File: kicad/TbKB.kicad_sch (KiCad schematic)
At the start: 320 parts, among them U1 NCP1117-3.3_SOT223, U2 W25Q128JVS, U3 RP2040, X1 USB Type C, Y1 ABLS-12.000MHZ-B4-T

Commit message: routing complete
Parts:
- added K_Space_2U_2: SW_SPST, keyswitches:Kailh_socket_MX_2.25u, symbol Switch:SW_SPST
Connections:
- net Col_3: now also K_Space_2U_2.2 (B)
- net at D33.2 (A), K_enter1.1 (A): now also K_Space_2U_2.1 (A)
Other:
- note added: "Make sure R7 and R8 are close to RP2040"
- note removed: "Make sure R3 and R4 are close to RP2040"
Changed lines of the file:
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@@
   (junction (at 402.59 294.64) (diameter 0) (color 0 0 0 0)
   )
+  (junction (at 360.68 175.26) (diameter 0) (color 0 0 0 0)
+  )
   (junction (at 320.04 182.88) (diameter 0) (color 0 0 0 0)
   )
@@
   (junction (at 396.24 139.7) (diameter 0) (color 0 0 0 0)
   )
+  (junction (at 350.52 175.26) (diameter 0) (color 0 0 0 0)
+  )
   (junction (at 615.95 407.67) (diameter 0) (color 0 0 0 0)
   )
@@
     (stroke (width 0) (type default) (color 0 0 0 0))
   )
+  (wire (pts (xy 350.52 191.77) (xy 344.17 191.77))
+    (stroke (width 0) (type default) (color 0 0 0 0))
+  )
   (wire (pts (xy 641.35 326.39) (xy 666.75 326.39))
     (stroke (width 0) (type default) (color 0 0 0 0))
@@
     (stroke (width 0) (type default) (color 0 0 0 0))
   )
+  (wire (pts (xy 360.68 175.26) (xy 360.68 191.77))
+    (stroke (width 0) (type default) (color 0 0 0 0))
+  )
   (wire (pts (xy 699.77 367.03) (xy 709.93 367.03))
     (stroke (width 0) (type default) (color 0 0 0 0))
@@
     (stroke (width 0) (type default) (color 0 0 0 0))
   )
+  (wire (pts (xy 344.17 191.77) (xy 344.17 175.26))
+    (stroke (width 0) (type default) (color 0 0 0 0))
+  )
   (wire (pts (xy 482.6 118.11) (xy 482.6 137.16))
     (stroke (width 0) (type default) (color 0 0 0 0))
@@
     (stroke (width 0) (type default) (color 0 0 0 0))
   )
+  (wire (pts (xy 344.17 175.26) (xy 350.52 175.26))
+    (stroke (width 0) (type default) (color 0 0 0 0))
+  )
   (wire (pts (xy 674.37 496.57) (xy 684.53 496.57))
     (stroke (width 0) (type default) (color 0 0 0 0))
@@
     (effects (font (size 2.54 2.54)) (justify left bottom))
   )
-  (text "Make sure R3 and R4 are close to RP2040" (at 408.94 322.58 0)
+  (text "Make sure R7 and R8 are close to RP2040" (at 408.94 322.58 0)
     (effects (font (size 1.27 1.27)) (justify left bottom))
   )
@@
     (pin "4")
   )
+  (symbol (lib_id "Switch:SW_SPST") (at 355.6 191.77 0) (unit 1)
+    (in_bom yes) (on_board yes) (fields_autoplaced)
+    (property "Reference" "K_Space_2U_2" (id 0) (at 355.6 185.42 0))
+    (property "Value" "SW_SPST" (id 1) (at 355.6 187.96 0))
+    (property "Footprint" "keyswitches:Kailh_socket_MX_2.25u" (id 2) (at 355.6 191.77 0)
+      (effects (font (size 1.27 1.27)) hide)
+    )
+    (property "Datasheet" "~" (id 3) (at 355.6 191.77 0)
+      (effects (font (size 1.27 1.27)) hide)
+    )
+    (pin "1")
+    (pin "2")
+  )
   (symbol (lib_id "Diode:1N4148W") (at 304.8 116.84 90) (unit 1)
     (in_bom yes) (on_board yes) (fields_autoplaced)
@@
       (reference "K_App1") (unit 1) (value "SW_SPST") (footprint "keyswitches:Kailh_socket_MX_1u")
     )
+    (path "/182656ee-5a69-4ef5-99ed-b9ed53404886"
+      (reference "K_Space_2U_2") (unit 1) (value "SW_SPST") (footprint "keyswitches:Kailh_socket_MX_2.25u")
+    )
     (path "/7c1d743f-2ed7-4b25-9d6a-c0a900bee7f4"

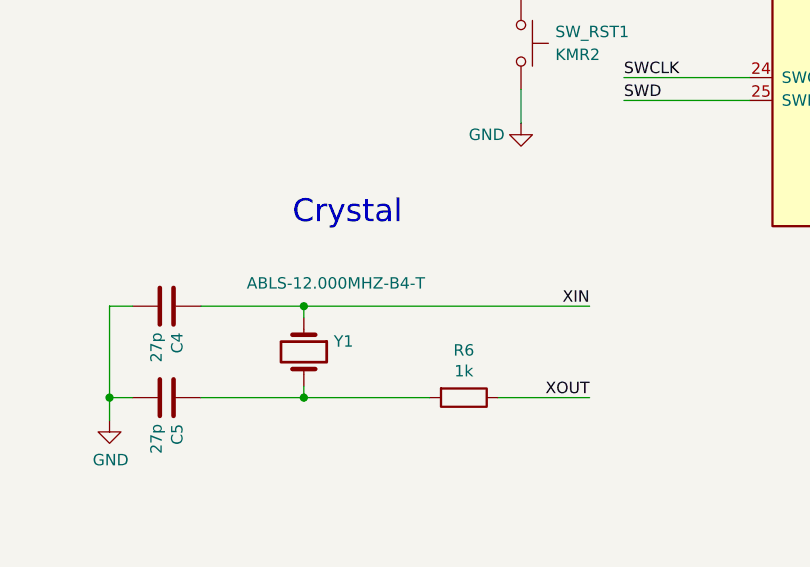
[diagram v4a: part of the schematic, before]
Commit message: added other 3d models, fixed crystal
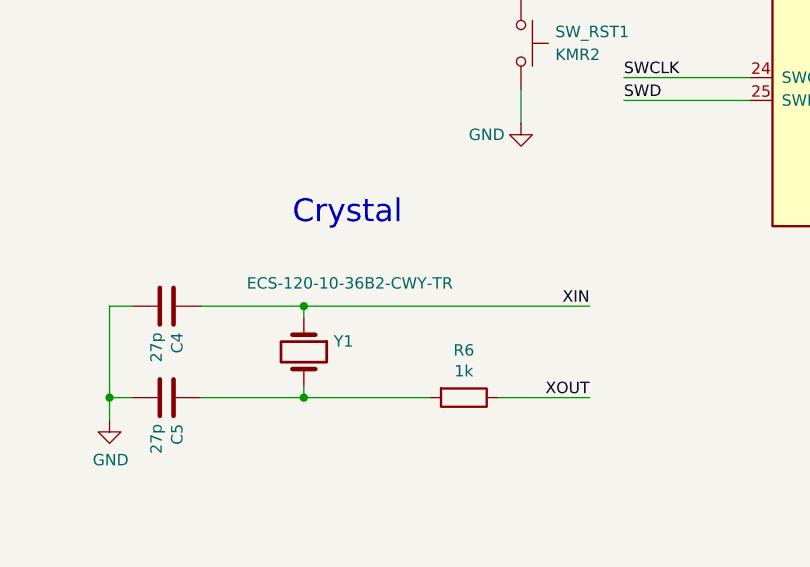
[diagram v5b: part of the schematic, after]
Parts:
- Y1: value ABLS-12.000MHZ-B4-T -> ‎ECS-120-10-36B2-CWY-TR‎; footprint RP2040_minimal:Crystal_SMD_HC49-US -> ECS-120:ECS-120-10-36B-CWY-TR
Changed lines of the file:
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@@
       (effects (font (size 1.27 1.27)) (justify left))
     )
-    (property "Value" "ABLS-12.000MHZ-B4-T" (id 1) (at 266.7 421.64 90)
+    (property "Value" "‎ECS-120-10-36B2-CWY-TR‎" (id 1) (at 266.7 421.64 90)
       (effects (font (size 1.27 1.27)) (justify left))
     )
-    (property "Footprint" "RP2040_minimal:Crystal_SMD_HC49-US" (id 2) (at 273.05 429.26 0)
+    (property "Footprint" "ECS-120:ECS-120-10-36B-CWY-TR" (id 2) (at 273.05 429.26 0)
       (effects (font (size 1.27 1.27)) hide)
     )
@@
     )
     (path "/41eb6801-d449-4bda-9c9f-c3f5d80fdad8"
-      (reference "Y1") (unit 1) (value "ABLS-12.000MHZ-B4-T") (footprint "RP2040_minimal:Crystal_SMD_HC49-US")
+      (reference "Y1") (unit 1) (value "‎ECS-120-10-36B2-CWY-TR‎") (footprint "ECS-120:ECS-120-10-36B-CWY-TR")
     )
   )

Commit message: update switch references to k_<n> values
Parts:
- renumbered K_esc1 to K_0, K_tilda1 to K_1, K_9 to K_10, K_0 to K_11, K_bkslash1 to K_12, K_del1 to K_13, K_-1 to K_14, K_=1 to K_15, K_tab1 to K_16, K_q1 to K_17, K_w1 to K_18, K_e1 to K_19, K_1 to K_2, K_r1 to K_20, K_t1 to K_21, K_y1 to K_22, K_u1 to K_23, K_i1 to K_24, K_o1 to K_25, K_p1 to K_26, K_bkspc1 to K_28, K_[1 to K_29, K_2 to K_3, K_]1 to K_30, K_ctrl1 to K_31, K_a1 to K_32, K_s1 to K_33, K_d1 to K_34, K_f1 to K_35, K_g1 to K_36, K_h1 to K_37, K_j1 to K_38, K_k1 to K_39, K_3 to K_4, K_l1 to K_40, K_;1 to K_41, K_'2 to K_42, K_return1 to K_43, K_'1 to K_45, K_home1 to K_46, K_lshift1 to K_47, K_z1 to K_48, K_x1 to K_49, K_4 to K_5, K_c1 to K_50, K_v1 to K_51, K_b1 to K_52, K_n1 to K_53, K_m1 to K_54, K_,1 to K_55, K_.1 to K_56, K_/1 to K_57, K_rshift1 to K_59, K_5 to K_6, K_end1 to K_60, K_up1 to K_61, K_fn1 to K_62, K_super1 to K_63, K_blank1 to K_64, K_Space_2U_2 to K_65, K_enter1 to K_66, K_App1 to K_67, K_Alt1 to K_68, K_Sys1 to K_69, K_6 to K_7, K_left1 to K_70, K_down1 to K_71, K_right1 to K_72, K_7 to K_8, K_8 to K_9, SW_RST1 to RESET, SW_USB_BOOT1 to USB_BOOT
